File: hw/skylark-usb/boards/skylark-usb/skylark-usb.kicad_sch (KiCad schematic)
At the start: 0 parts

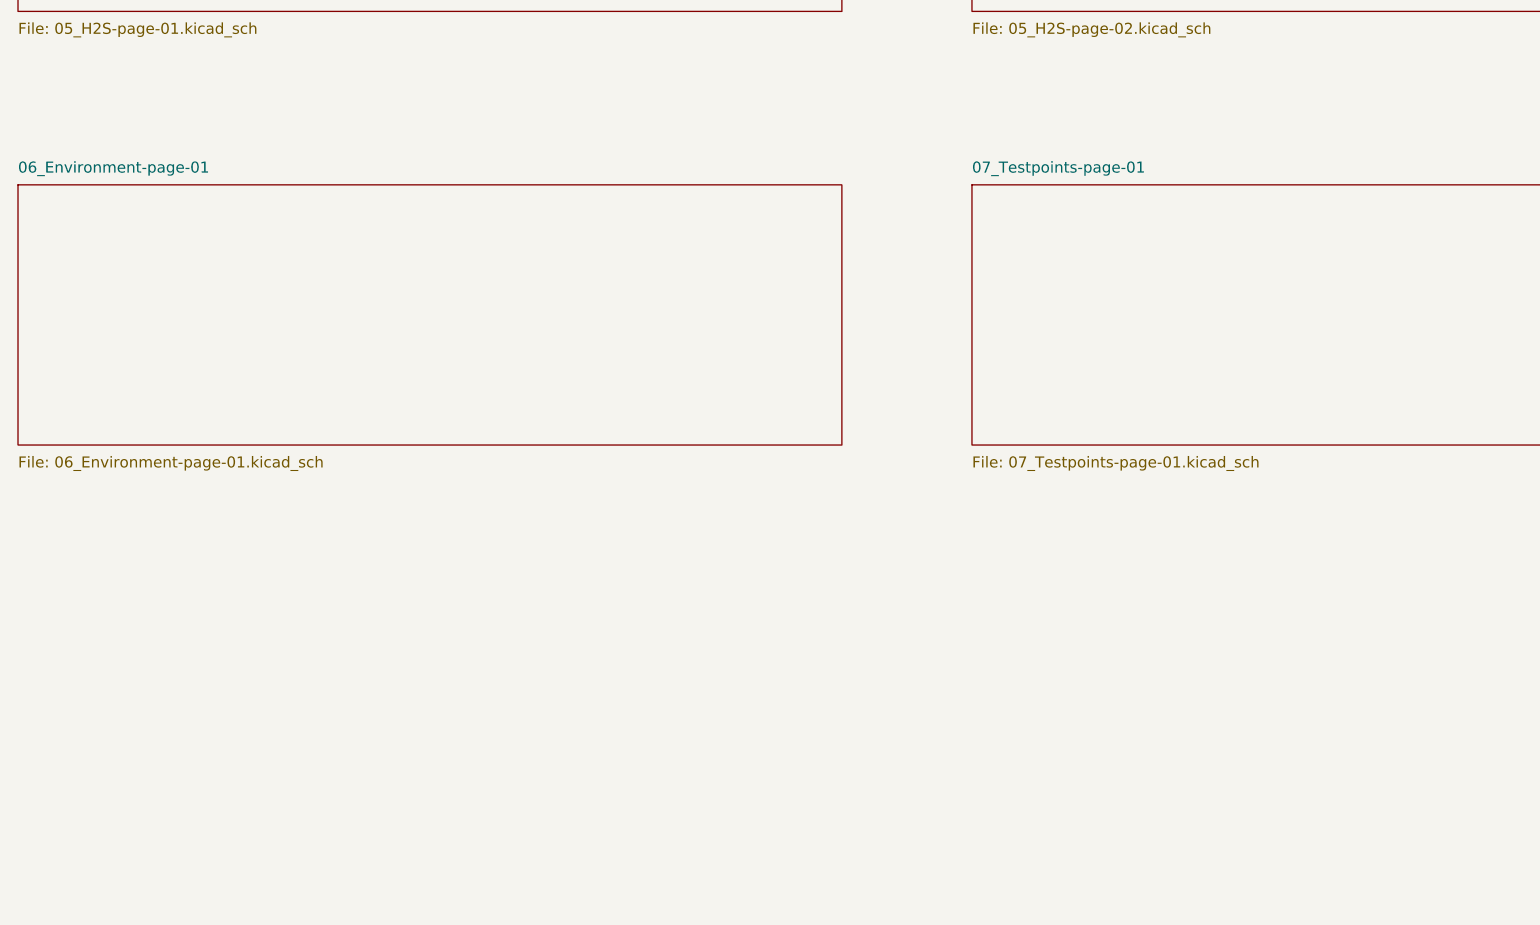
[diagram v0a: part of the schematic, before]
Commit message: Harden Skylark signal chain and add manufacturing audit
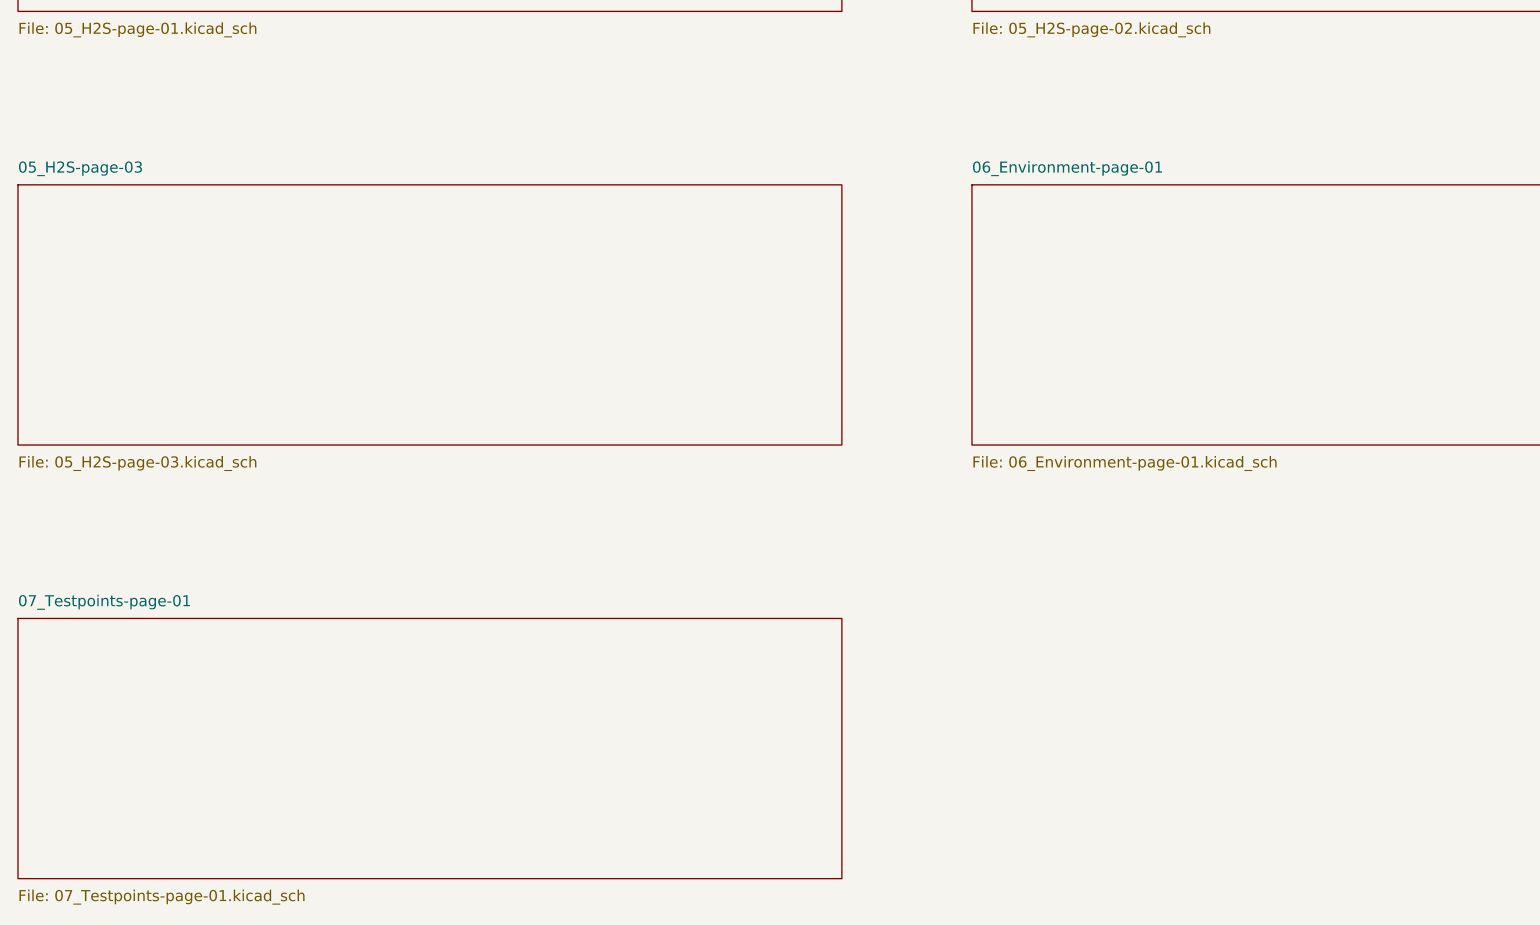
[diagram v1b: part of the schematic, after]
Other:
- added sheet 05_H2S-page-03 (05_H2S-page-03.kicad_sch)
